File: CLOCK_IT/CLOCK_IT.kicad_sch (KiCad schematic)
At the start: 0 parts

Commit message: :tada: Completed mcu.. minor fixes to be done
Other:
- added sheet MCU (mcu.kicad_sch)
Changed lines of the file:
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@@
 	(generator_version "9.0")
 	(paper "A4")
+	(sheet
+		(at 110.49 54.61)
+		(size 27.94 26.67)
+		(exclude_from_sim no)
+		(in_bom yes)
+		(on_board yes)
+		(dnp no)
+		(fields_autoplaced yes)
+		(stroke
+			(width 0.1524)
+			(type solid)
+		)
+		(fill
+			(color 0 0 0 0.0000)
+		)
+		(property "Sheetname" "MCU"
+			(at 110.49 53.8984 0)
+			(effects
+				(font
+					(size 1.27 1.27)
+				)
+				(justify left bottom)
+			)
+		)
+		(property "Sheetfile" "mcu.kicad_sch"
+			(at 110.49 81.8646 0)
+			(effects
+				(font
+					(size 1.27 1.27)
+				)
+				(justify left top)
+			)
+		)
+		(instances
+			(project "CLOCK_IT"
+				(path "/6c8f4e2a-0be1-4eb1-92e1-07339040f4c9"
+					(page "2")
+				)
+			)
+		)
+	)
 	(sheet_instances
 		(path "/"

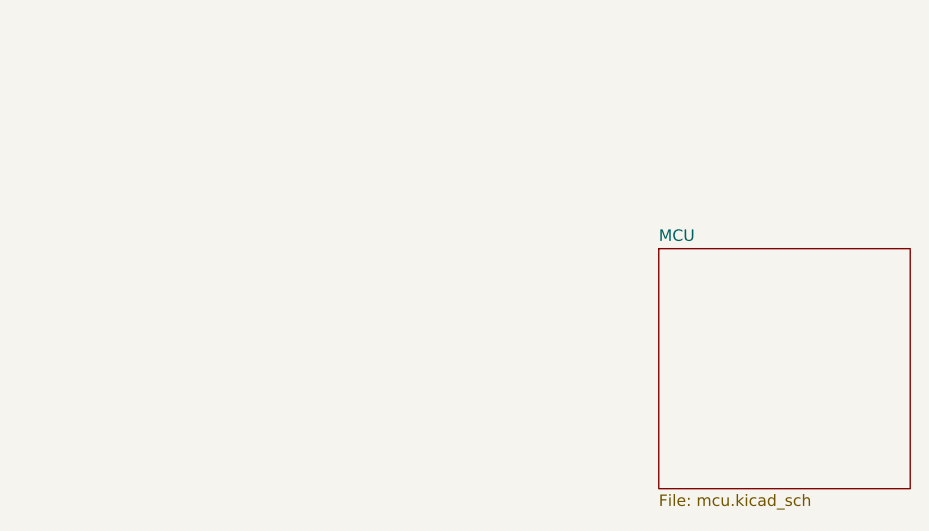
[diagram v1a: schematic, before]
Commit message: :memo:added SD CARD-TF-
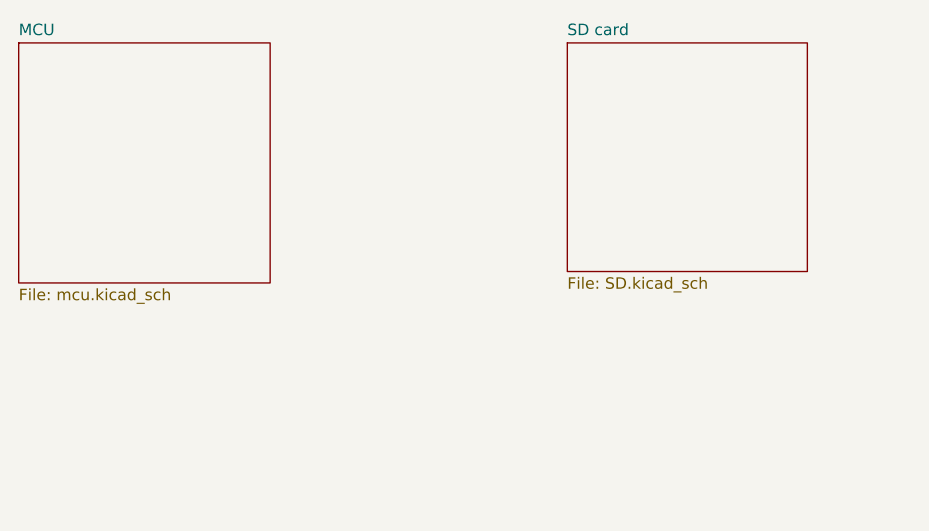
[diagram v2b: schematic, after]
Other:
- added sheet SD card (SD.kicad_sch)
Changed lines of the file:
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@@
 	(paper "A4")
 	(sheet
-		(at 110.49 54.61)
+		(at 39.37 31.75)
 		(size 27.94 26.67)
 		(exclude_from_sim no)
@@
 		)
 		(property "Sheetname" "MCU"
-			(at 110.49 53.8984 0)
+			(at 39.37 31.0384 0)
 			(effects
 				(font
@@
 		)
 		(property "Sheetfile" "mcu.kicad_sch"
-			(at 110.49 81.8646 0)
+			(at 39.37 59.0046 0)
 			(effects
 				(font
@@
 				)
 			)
+		)
+	)
+	(sheet
+		(at 100.33 31.75)
+		(size 26.67 25.4)
+		(exclude_from_sim no)
+		(in_bom yes)
+		(on_board yes)
+		(dnp no)
+		(fields_autoplaced yes)
+		(stroke
+			(width 0.1524)
+			(type solid)
+		)
+		(fill
+			(color 0 0 0 0.0000)
+		)
+		(property "Sheetname" "SD card"
+			(at 100.33 31.0384 0)
+			(effects
+				(font
+					(size 1.27 1.27)
+				)
+				(justify left bottom)
+			)
+		)
+		(property "Sheetfile" "SD.kicad_sch"
+			(at 100.33 57.7346 0)
+			(effects
+				(font
+					(size 1.27 1.27)
+				)
+				(justify left top)
+			)
+		)
+		(instances
+			(project "CLOCK_IT"
+				(path "/6c8f4e2a-0be1-4eb1-92e1-07339040f4c9"
+					(page "3")
+				)
+			)
